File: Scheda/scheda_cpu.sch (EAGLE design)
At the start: 8 parts

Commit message: varie robe
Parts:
- removed ROCKET: CONNECTOR-6, CiniTechLibrary:CONNECTOR-6
- added R1, R2, R3, R4: 10k, CiniTechLibrary:RESISTOR1206
- added SERVO: CONNECTOR-61X6-CONNECTOR-90°, CiniTechLibrary:CONNECTOR-61X6-CONNECTOR-90°
- added U$1, U$2, U$3, U$4: MCU80N03A, CiniTechLibrary:MCU80N03A
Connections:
- removed net N$10: IC1.A5, ROCKET.P$6
- removed net N$5: IC1.A0, ROCKET.P$1
- removed net N$6: IC1.A1, ROCKET.P$2
- removed net N$7: IC1.A2, ROCKET.P$3
- removed net N$8: IC1.A3, ROCKET.P$4
- removed net N$9: IC1.A4, ROCKET.P$5
- new net C_R0: IC1.A0, R1.P$2, U$1.G
- new net C_R1: IC1.A1, R2.P$2, U$2.G
- new net C_R2: IC1.A2, R3.P$2, U$3.G
- new net C_R3: IC1.A3, R4.P$2, U$4.G
- new net R0: U$1.D
- new net R1: U$2.D
- new net R2: U$3.D
- new net R3: U$4.D
- new net SERVO1: IC1.D5, SERVO.P$3
- new net SERVO2: IC1.D6, SERVO.P$6
- net +5V: now also SERVO.P$2, SERVO.P$5
- net GND: now also R1.P$1, R2.P$1, R3.P$1, R4.P$1, SERVO.P$1, SERVO.P$4, U$1.S, U$2.S, U$3.S, U$4.S
- net N$2: now also IC1.RX0; no longer IC1.D4
- net N$3: now also IC1.TX1; no longer IC1.D5
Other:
- moved on the sheet: MP3, SUP1, SUP2, SUP3

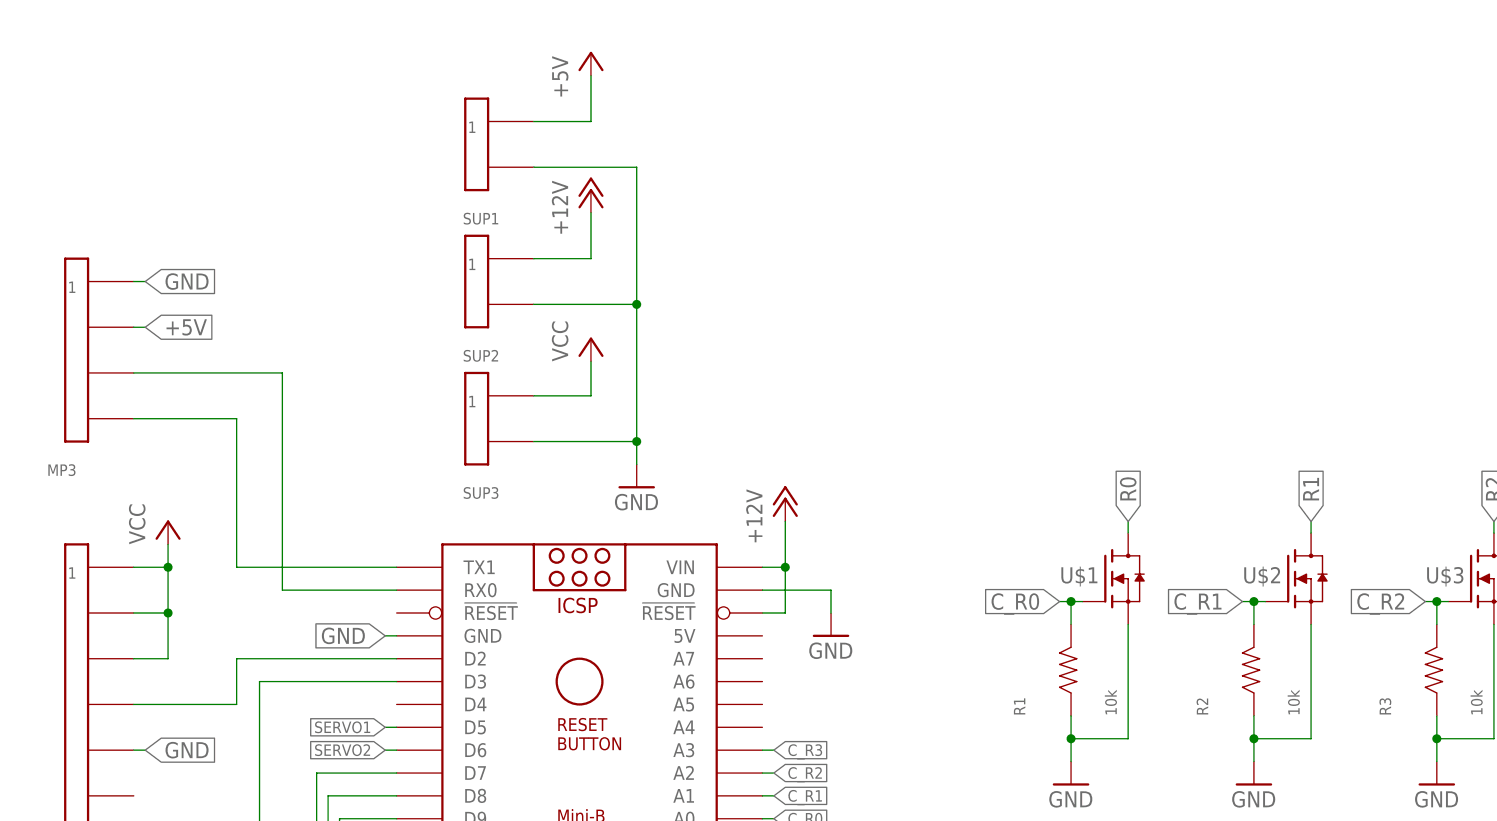
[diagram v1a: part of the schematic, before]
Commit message: creata la libreria roombarmato_eagle_lib che verrà usata per tenere tutti i componenti presenti sulla scheda, aggiunti regolatori di tensione per la generazione di +5v e +3.3
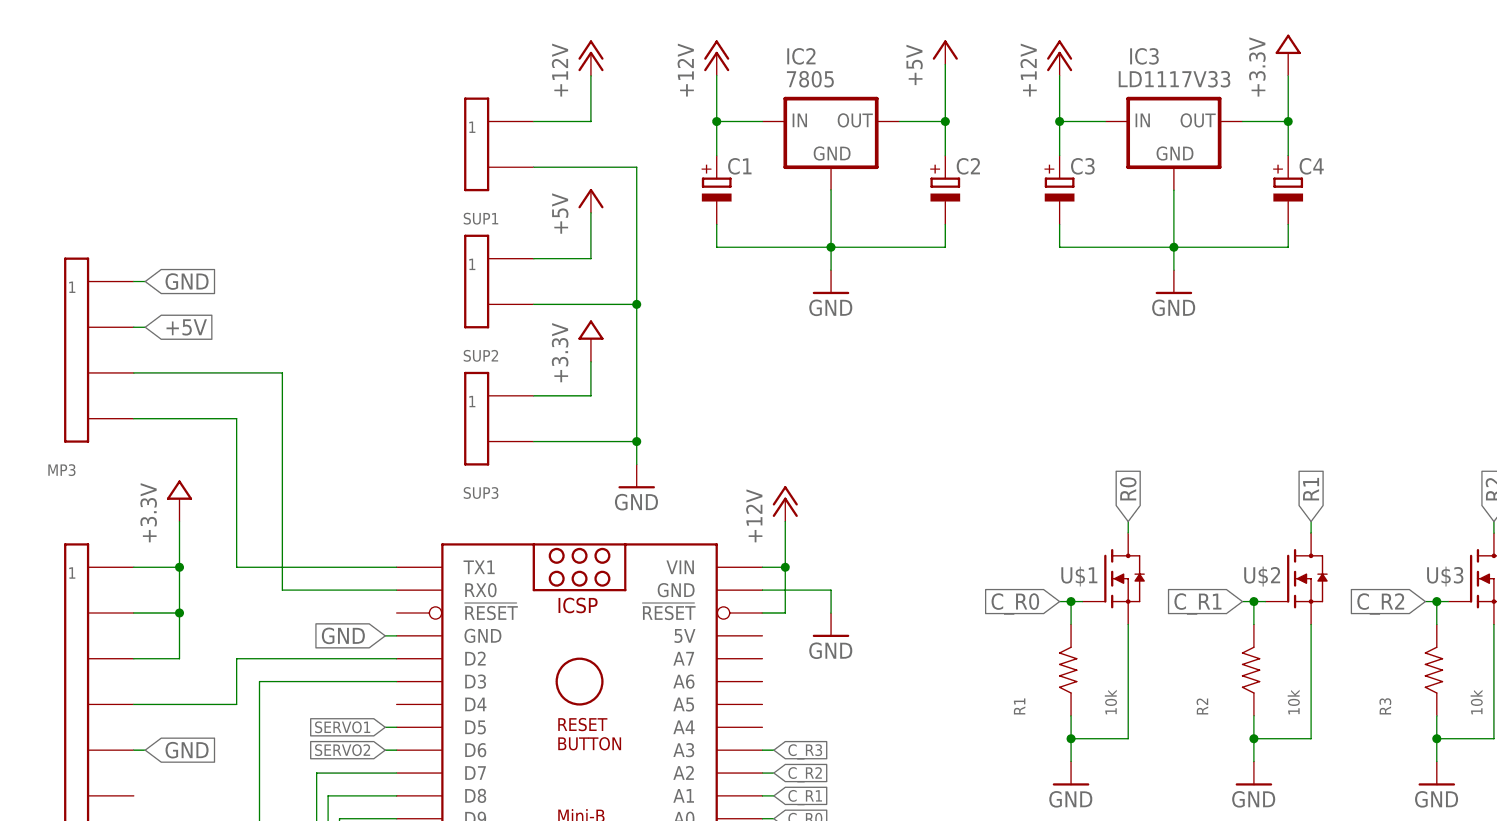
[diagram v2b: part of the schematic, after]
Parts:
- added C1, C2, C3, C4: (no value), roombarmato_eagle_lib:CPOL-EUE2.5-5
- added IC2: 7805, roombarmato_eagle_lib:78XXS
- added IC3: LD1117V33, roombarmato_eagle_lib:78XXS
- ESP: device CiniTechLibrary:CONNECTOR-82X4-CONNECTOR -> roombarmato_eagle_lib:CONNECTOR-82X4-CONNECTOR
- IC1: device CiniTechLibrary:ARDUINO-NANO -> roombarmato_eagle_lib:ARDUINO-NANO
- MOTORS: device CiniTechLibrary:CONNECTOR-6 -> roombarmato_eagle_lib:CONNECTOR-6
- MP3: device CiniTechLibrary:CONNECTOR-4 -> roombarmato_eagle_lib:CONNECTOR-4
- R1, R2, R3, R4: device CiniTechLibrary:RESISTOR1206 -> roombarmato_eagle_lib:RESISTOR1206
- SERVO: value CONNECTOR-61X6-CONNECTOR-90° -> CONNECTOR-6; device CiniTechLibrary:CONNECTOR-61X6-CONNECTOR-90° -> roombarmato_eagle_lib:CONNECTOR-6
- SUP1, SUP2, SUP3: device CiniTechLibrary:AK500 -> roombarmato_eagle_lib:AK500
- U$1, U$2, U$3, U$4: device CiniTechLibrary:MCU80N03A -> roombarmato_eagle_lib:MCU80N03A
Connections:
- removed net VCC: ESP.P$1, ESP.P$2, ESP.P$3, SUP3.P$1
- net +12V: now also C1.+, C3.+, IC2.IN, IC3.IN, SUP1.P$1; no longer SUP2.P$1
- net +5V: now also C2.+, C4.+, ESP.P$1, ESP.P$2, ESP.P$3, IC2.OUT, IC3.OUT, SUP2.P$1, SUP3.P$1; no longer SUP1.P$1
- net GND: now also C1.-, C2.-, C3.-, C4.-, IC2.GND, IC3.GND

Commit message: creato il pcb di prova
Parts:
- added ROCKETS: MORSETTIERE-4, roombarmato_eagle_lib:MORSETTIERE-4
- renumbered SUP1 to SUP_12, SUP2 to SUP_5, SUP3 to SUP_3
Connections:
- new net +3.3V: C4.+, ESP.P$1, ESP.P$2, ESP.P$3, IC3.OUT, SUP_3.P$1
- net +12V: no longer IC1.!RESET@2
- net +5V: no longer C4.+, ESP.P$1, ESP.P$2, ESP.P$3, IC3.OUT, SUP_3.P$1
- net R0: now also ROCKETS.D
- net R1: now also ROCKETS.C
- net R2: now also ROCKETS.B
- net R3: now also ROCKETS.A
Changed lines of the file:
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@@
 <part name="GND2" library="roombarmato_eagle_lib" deviceset="GND" device=""/>
 <part name="MP3" library="roombarmato_eagle_lib" deviceset="CONNECTOR-4" device="" package3d_urn="urn:adsk.eagle:package:17815777/5"/>
-<part name="SUP3" library="roombarmato_eagle_lib" deviceset="AK500" device="" package3d_urn="urn:adsk.eagle:package:17855270/2"/>
-<part name="SUP2" library="roombarmato_eagle_lib" deviceset="AK500" device="" package3d_urn="urn:adsk.eagle:package:17855270/2"/>
-<part name="SUP1" library="roombarmato_eagle_lib" deviceset="AK500" device="" package3d_urn="urn:adsk.eagle:package:17855270/2"/>
+<part name="SUP_3" library="roombarmato_eagle_lib" deviceset="AK500" device="" package3d_urn="urn:adsk.eagle:package:17855270/2"/>
+<part name="SUP_5" library="roombarmato_eagle_lib" deviceset="AK500" device="" package3d_urn="urn:adsk.eagle:package:17855270/2"/>
+<part name="SUP_12" library="roombarmato_eagle_lib" deviceset="AK500" device="" package3d_urn="urn:adsk.eagle:package:17855270/2"/>
 <part name="P+4" library="roombarmato_eagle_lib" deviceset="+12V" device=""/>
 <part name="GND1" library="roombarmato_eagle_lib" deviceset="GND" device=""/>
@@
 <part name="P+9" library="roombarmato_eagle_lib" deviceset="+3.3V" device=""/>
 <part name="GND8" library="roombarmato_eagle_lib" deviceset="GND" device=""/>
+<part name="ROCKETS" library="roombarmato_eagle_lib" deviceset="MORSETTIERE-4" device=""/>
 </parts>
 <sheets>
@@
 <attribute name="NAME" x="-55.88" y="24.13" size="1.27" layer="95" rot="R180"/>
 </instance>
-<instance part="SUP3" gate="G$1" x="-11.43" y="29.21" smashed="yes" rot="R180">
-<attribute name="NAME" x="-8.89" y="21.59" size="1.27" layer="95" rot="R180"/>
-</instance>
-<instance part="SUP2" gate="G$1" x="-11.43" y="44.45" smashed="yes" rot="R180">
-<attribute name="NAME" x="-8.89" y="36.83" size="1.27" layer="95" rot="R180"/>
-</instance>
-<instance part="SUP1" gate="G$1" x="-11.43" y="59.69" smashed="yes" rot="R180">
-<attribute name="NAME" x="-8.89" y="52.07" size="1.27" layer="95" rot="R180"/>
+<instance part="SUP_3" gate="G$1" x="-11.43" y="29.21" smashed="yes" rot="R180">
+<attribute name="NAME" x="-8.89" y="22.86" size="1.27" layer="95" rot="R180"/>
+</instance>
+<instance part="SUP_5" gate="G$1" x="-11.43" y="44.45" smashed="yes" rot="R180">
+<attribute name="NAME" x="-8.89" y="38.1" size="1.27" layer="95" rot="R180"/>
+</instance>
+<instance part="SUP_12" gate="G$1" x="-11.43" y="59.69" smashed="yes" rot="R180">
+<attribute name="NAME" x="-8.89" y="53.34" size="1.27" layer="95" rot="R180"/>
 </instance>
 <instance part="P+4" gate="1" x="1.27" y="69.85" smashed="yes">
@@
 <instance part="GND8" gate="1" x="66.04" y="43.18" smashed="yes">
 <attribute name="VALUE" x="63.5" y="40.64" size="1.778" layer="96"/>
+</instance>
+<instance part="ROCKETS" gate="G$1" x="95.25" y="27.94" smashed="yes" rot="R180">
+<attribute name="NAME" x="95.25" y="43.18" size="1.778" layer="95" rot="R180"/>
 </instance>
 </instances>
@@
 <pinref part="P+2" gate="1" pin="+12V"/>
 <wire x1="22.86" y1="12.7" x2="22.86" y2="17.78" width="0.1524" layer="91"/>
-<pinref part="IC1" gate="G$1" pin="!RESET@2"/>
-<wire x1="20.32" y1="7.62" x2="22.86" y2="7.62" width="0.1524" layer="91"/>
-<wire x1="22.86" y1="7.62" x2="22.86" y2="12.7" width="0.1524" layer="91"/>
-<junction x="22.86" y="12.7"/>
-</segment>
-<segment>
-<pinref part="SUP1" gate="G$1" pin="P$1"/>
+</segment>
+<segment>
+<pinref part="SUP_12" gate="G$1" pin="P$1"/>
 <pinref part="P+4" gate="1" pin="+12V"/>
 <wire x1="-5.08" y1="62.23" x2="1.27" y2="62.23" width="0.1524" layer="91"/>
@@
 </segment>
 <segment>
-<pinref part="SUP3" gate="G$1" pin="P$2"/>
+<pinref part="SUP_3" gate="G$1" pin="P$2"/>
 <wire x1="-5.08" y1="26.67" x2="6.35" y2="26.67" width="0.1524" layer="91"/>
 <wire x1="6.35" y1="26.67" x2="6.35" y2="24.13" width="0.1524" layer="91"/>
 <pinref part="GND1" gate="1" pin="GND"/>
-<pinref part="SUP1" gate="G$1" pin="P$2"/>
+<pinref part="SUP_12" gate="G$1" pin="P$2"/>
 <wire x1="-5.08" y1="57.15" x2="6.35" y2="57.15" width="0.1524" layer="91"/>
 <wire x1="6.35" y1="57.15" x2="6.35" y2="41.91" width="0.1524" layer="91"/>
 <junction x="6.35" y="26.67"/>
-<pinref part="SUP2" gate="G$1" pin="P$2"/>
+<pinref part="SUP_5" gate="G$1" pin="P$2"/>
 <wire x1="6.35" y1="41.91" x2="6.35" y2="26.67" width="0.1524" layer="91"/>
 <wire x1="-5.08" y1="41.91" x2="6.35" y2="41.91" width="0.1524" layer="91"/>
@@
 </segment>
 <segment>
-<pinref part="SUP3" gate="G$1" pin="P$1"/>
-<pinref part="P+3" gate="G$1" pin="+5V"/>
-<wire x1="-5.08" y1="31.75" x2="1.27" y2="31.75" width="0.1524" layer="91"/>
-<wire x1="1.27" y1="31.75" x2="1.27" y2="35.56" width="0.1524" layer="91"/>
-</segment>
-<segment>
-<pinref part="SUP2" gate="G$1" pin="P$1"/>
+<pinref part="SUP_5" gate="G$1" pin="P$1"/>
 <pinref part="P+1" gate="1" pin="+5V"/>
 <wire x1="-5.08" y1="46.99" x2="1.27" y2="46.99" width="0.1524" layer="91"/>
 <wire x1="1.27" y1="46.99" x2="1.27" y2="52.07" width="0.1524" layer="91"/>
-</segment>
-<segment>
-<pinref part="ESP" gate="G$1" pin="P$1"/>
-<pinref part="P+5" gate="G$1" pin="+5V"/>
-<wire x1="-49.53" y1="12.7" x2="-44.45" y2="12.7" width="0.1524" layer="91"/>
-<wire x1="-44.45" y1="12.7" x2="-44.45" y2="17.78" width="0.1524" layer="91"/>
-<pinref part="ESP" gate="G$1" pin="P$2"/>
-<wire x1="-49.53" y1="7.62" x2="-44.45" y2="7.62" width="0.1524" layer="91"/>
-<wire x1="-44.45" y1="7.62" x2="-44.45" y2="12.7" width="0.1524" layer="91"/>
-<junction x="-44.45" y="12.7"/>
-<pinref part="ESP" gate="G$1" pin="P$3"/>
-<wire x1="-49.53" y1="2.54" x2="-44.45" y2="2.54" width="0.1524" layer="91"/>
-<wire x1="-44.45" y1="2.54" x2="-44.45" y2="7.62" width="0.1524" layer="91"/>
-<junction x="-44.45" y="7.62"/>
 </segment>
 <segment>
@@
 <wire x1="40.64" y1="62.23" x2="40.64" y2="68.58" width="0.1524" layer="91"/>
 </segment>
-<segment>
-<pinref part="IC3" gate="1" pin="OUT"/>
-<wire x1="73.66" y1="62.23" x2="78.74" y2="62.23" width="0.1524" layer="91"/>
-<wire x1="78.74" y1="62.23" x2="78.74" y2="58.42" width="0.1524" layer="91"/>
-<pinref part="C4" gate="G$1" pin="+"/>
-<pinref part="P+9" gate="G$1" pin="+5V"/>
-<wire x1="78.74" y1="62.23" x2="78.74" y2="67.31" width="0.1524" layer="91"/>
-<junction x="78.74" y="62.23"/>
-</segment>
 </net>
 <net name="N$2" class="0">
@@
 <label x="60.96" y="17.78" size="1.778" layer="95" rot="R90" xref="yes"/>
 </segment>
+<segment>
+<pinref part="ROCKETS" gate="G$1" pin="D"/>
+<wire x1="87.63" y1="38.1" x2="86.36" y2="38.1" width="0.1524" layer="91"/>
+<label x="86.36" y="38.1" size="1.27" layer="95" rot="R180" xref="yes"/>
+</segment>
 </net>
 <net name="R1" class="0">
@@
 <label x="81.28" y="17.78" size="1.778" layer="95" rot="R90" xref="yes"/>
 </segment>
+<segment>
+<pinref part="ROCKETS" gate="G$1" pin="C"/>
+<wire x1="87.63" y1="35.56" x2="86.36" y2="35.56" width="0.1524" layer="91"/>
+<label x="86.36" y="35.56" size="1.27" layer="95" rot="R180" xref="yes"/>
+</segment>
 </net>
 <net name="R2" class="0">
@@
 <label x="101.6" y="17.78" size="1.778" layer="95" rot="R90" xref="yes"/>
 </segment>
+<segment>
+<pinref part="ROCKETS" gate="G$1" pin="B"/>
+<wire x1="87.63" y1="33.02" x2="86.36" y2="33.02" width="0.1524" layer="91"/>
+<label x="86.36" y="33.02" size="1.27" layer="95" rot="R180" xref="yes"/>
+</segment>
 </net>
 <net name="R3" class="0">
@@
 <label x="121.92" y="17.78" size="1.778" layer="95" rot="R90" xref="yes"/>
 </segment>
+<segment>
+<pinref part="ROCKETS" gate="G$1" pin="A"/>
+<wire x1="87.63" y1="30.48" x2="86.36" y2="30.48" width="0.1524" layer="91"/>
+<label x="86.36" y="30.48" size="1.27" layer="95" rot="R180" xref="yes"/>
+</segment>
+</net>
+<net name="+3.3V" class="0">
+<segment>
+<pinref part="IC3" gate="1" pin="OUT"/>
+<wire x1="73.66" y1="62.23" x2="78.74" y2="62.23" width="0.1524" layer="91"/>
+<wire x1="78.74" y1="62.23" x2="78.74" y2="67.31" width="0.1524" layer="91"/>
+<pinref part="P+9" gate="G$1" pin="+3.3V"/>
+<pinref part="C4" gate="G$1" pin="+"/>
+<wire x1="78.74" y1="62.23" x2="78.74" y2="58.42" width="0.1524" layer="91"/>
+<junction x="78.74" y="62.23"/>
+</segment>
+<segment>
+<pinref part="ESP" gate="G$1" pin="P$1"/>
+<wire x1="-49.53" y1="12.7" x2="-44.45" y2="12.7" width="0.1524" layer="91"/>
+<wire x1="-44.45" y1="12.7" x2="-44.45" y2="7.62" width="0.1524" layer="91"/>
+<pinref part="ESP" gate="G$1" pin="P$3"/>
+<wire x1="-44.45" y1="7.62" x2="-44.45" y2="2.54" width="0.1524" layer="91"/>
+<wire x1="-44.45" y1="2.54" x2="-49.53" y2="2.54" width="0.1524" layer="91"/>
+<pinref part="ESP" gate="G$1" pin="P$2"/>
+<wire x1="-49.53" y1="7.62" x2="-44.45" y2="7.62" width="0.1524" layer="91"/>
+<junction x="-44.45" y="7.62"/>
+<pinref part="P+5" gate="G$1" pin="+3.3V"/>
+<wire x1="-44.45" y1="12.7" x2="-44.45" y2="17.78" width="0.1524" layer="91"/>
+<junction x="-44.45" y="12.7"/>
+</segment>
+<segment>
+<pinref part="P+3" gate="G$1" pin="+3.3V"/>
+<wire x1="1.27" y1="31.75" x2="1.27" y2="35.56" width="0.1524" layer="91"/>
+<pinref part="SUP_3" gate="G$1" pin="P$1"/>
+<wire x1="-5.08" y1="31.75" x2="1.27" y2="31.75" width="0.1524" layer="91"/>
+</segment>
 </net>
 </nets>
 </sheet>
 </sheets>
+<errors>
+</errors>
 </schematic>
 </drawing>

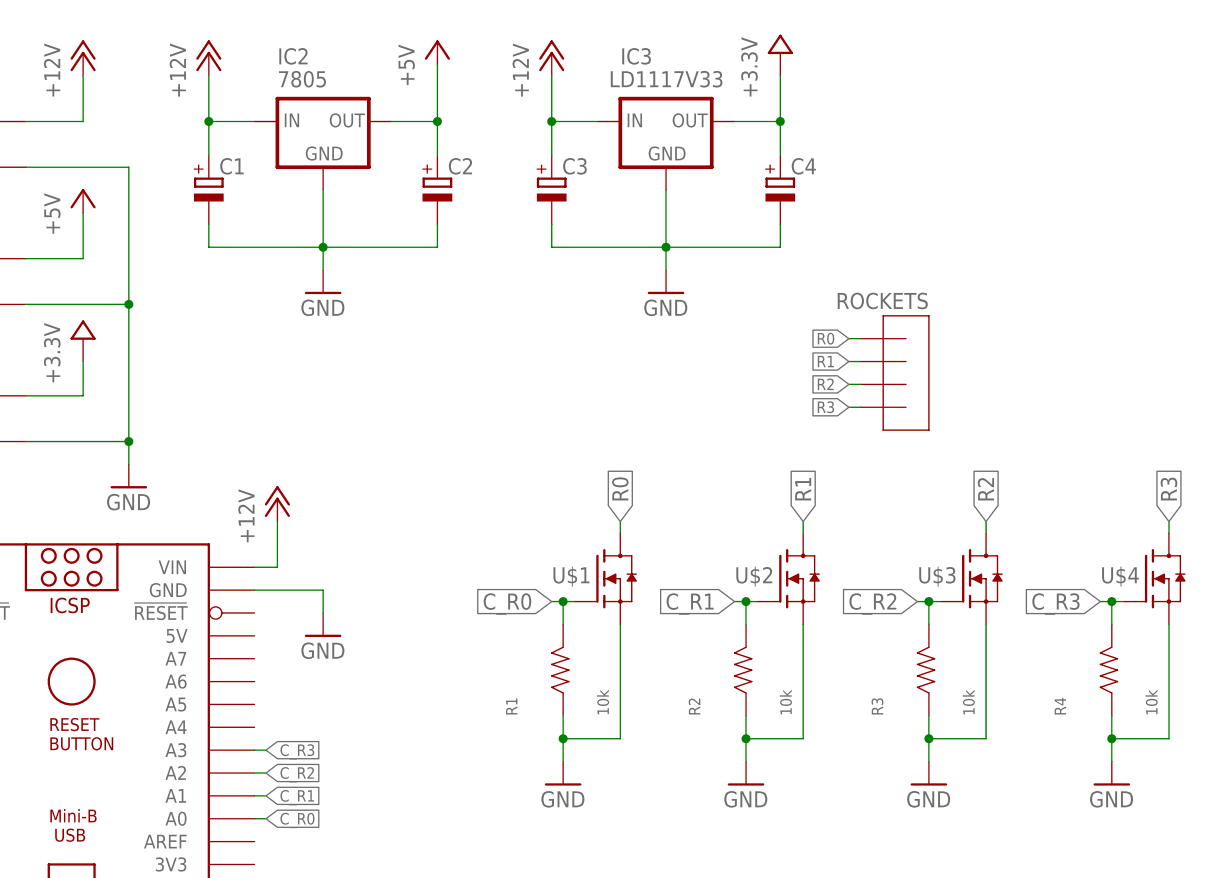
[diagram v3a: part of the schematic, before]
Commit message: modificato il sistema di accensione
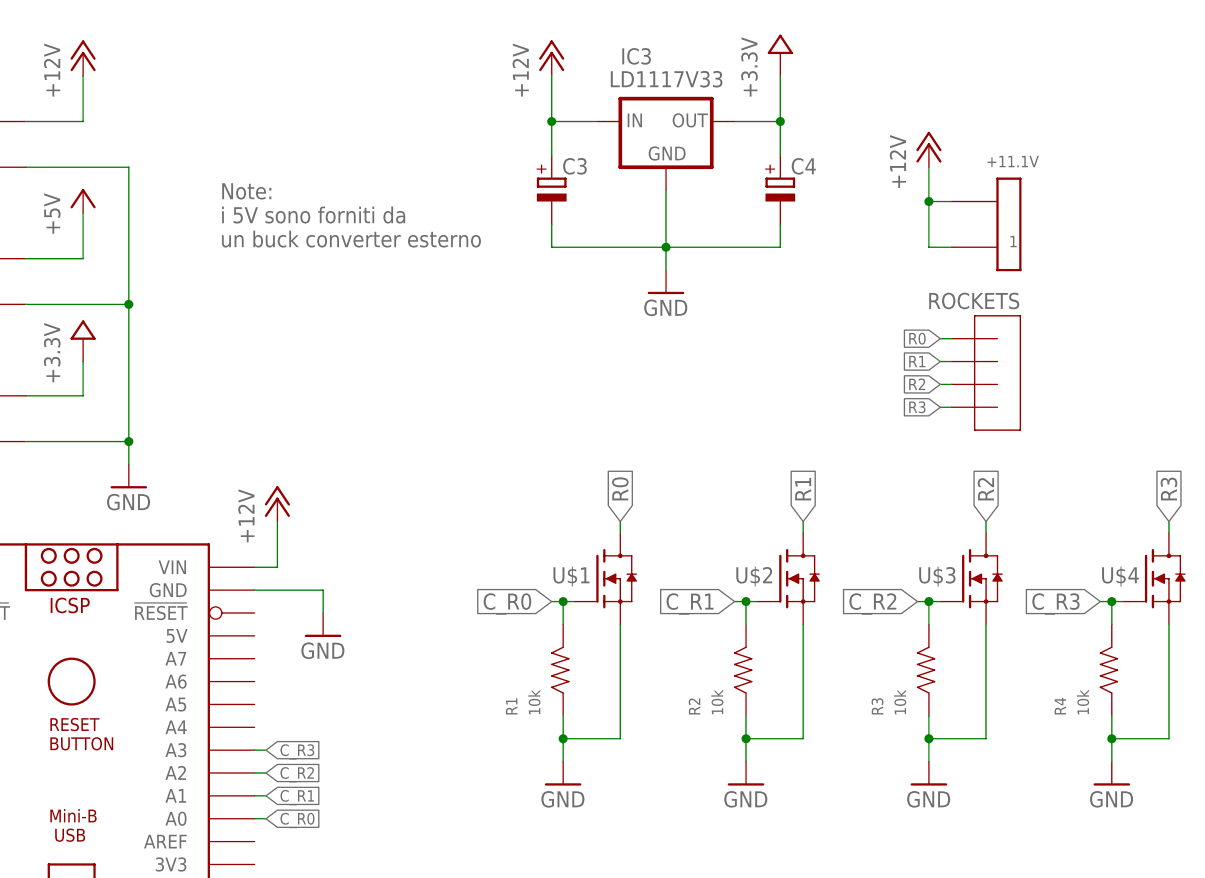
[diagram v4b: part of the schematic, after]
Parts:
- removed C1, C2: (no value), roombarmato_eagle_lib:CPOL-EUE2.5-5
- removed IC2: 7805, roombarmato_eagle_lib:78XXS
- added +11.1V: AK500, roombarmato_eagle_lib:AK500
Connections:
- net +12V: now also +11.1V.P$1, +11.1V.P$2; no longer C1.+, IC2.IN
- net +5V: no longer C2.+, IC2.OUT
- net GND: no longer C1.-, C2.-, IC2.GND
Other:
- note added: "Note: i 5V sono forniti da un buck converter esterno"
- moved on the sheet: ROCKETS
